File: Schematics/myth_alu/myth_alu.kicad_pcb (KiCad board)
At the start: 2 copper layers, 29 parts, among them J1 Conn_01x08_Pin, J2 Conn_01x08_Pin, J3 Conn_01x08_Pin, J4 Conn_01x08_Pin, J5 Conn_01x08_Pin, J6 Conn_01x08_Pin, J7 Conn_01x08_Pin, U1 74AHC273, U10 74AHC244, U11 74HC283, U12 74HC283, U13 74HC157, U14 74HC157, U15 74LS32, U16 74AHC273, U17 74AHC244, U18 4075, U19 74HC157, U2 74AHC273, U20 74HC283, U21 74HC283, U22 74AHC574, U3 SST39SF040, U4 74HC04, U5 SST39SF040, U6 74LS21, U7 74LS08, U8 74AHC273, U9 4078

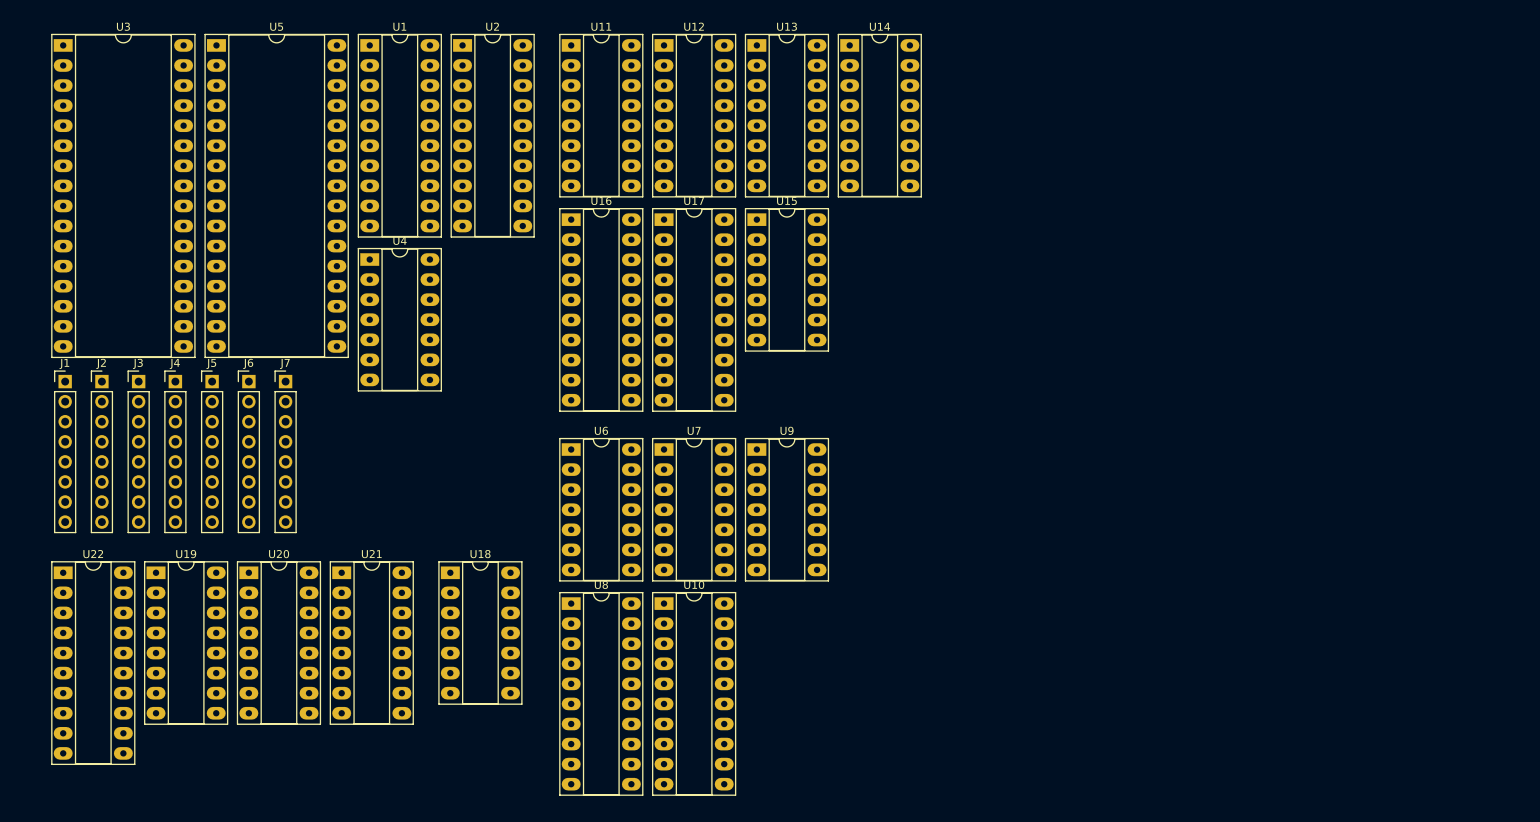
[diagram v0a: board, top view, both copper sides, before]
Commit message: Change d to g
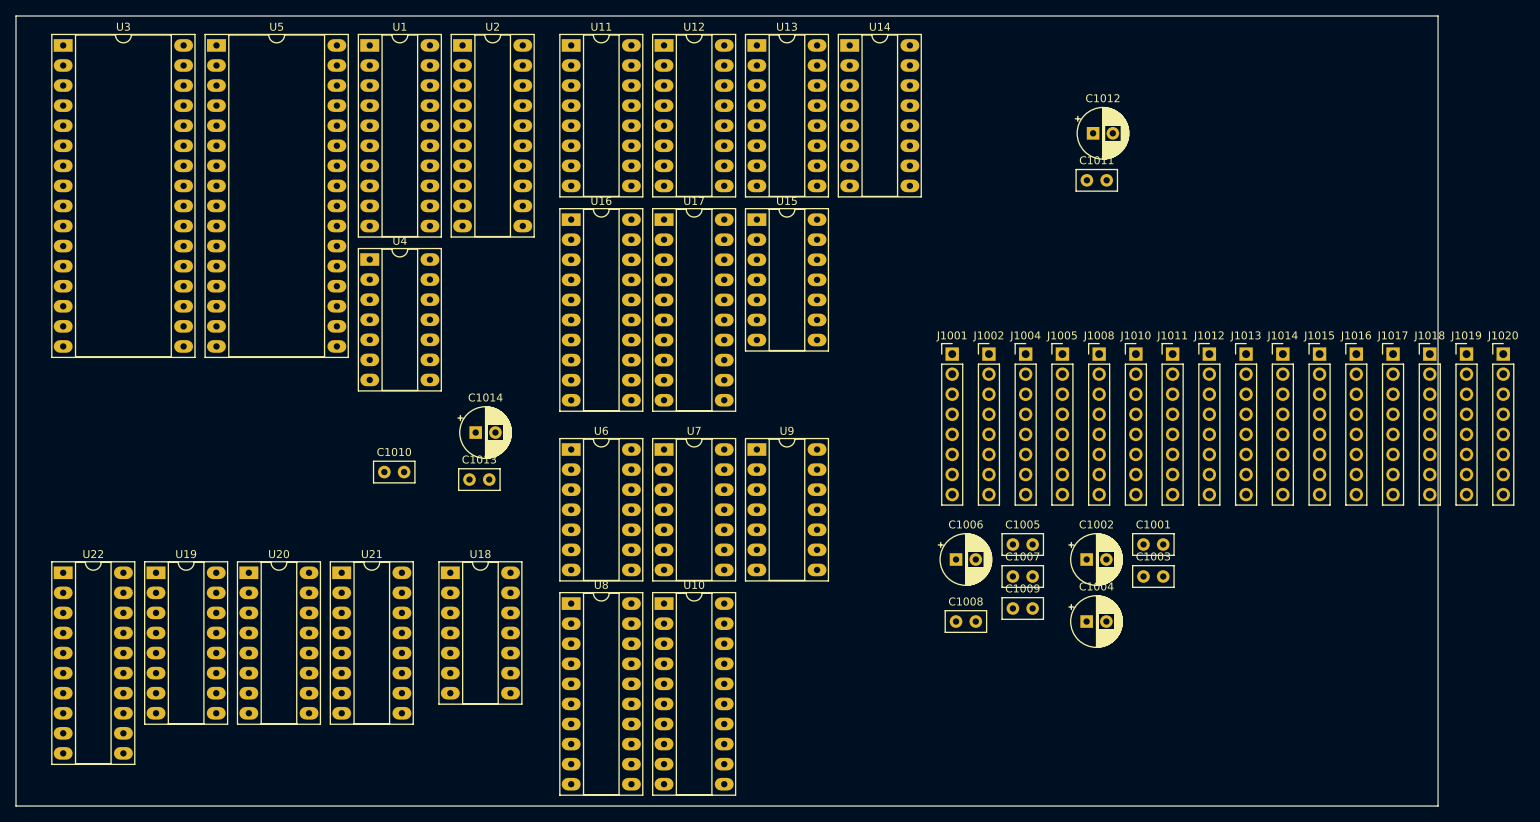
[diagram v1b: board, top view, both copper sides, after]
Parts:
- removed J1, J2, J3, J4, J5, J6, J7: Conn_01x08_Pin, Connector_PinHeader_2.54mm:PinHeader_1x08_P2.54mm_Vertical
- added C1001: C 100nF, Capacitor_THT:C_Disc_D5.0mm_W2.5mm_P2.50mm, F.Cu at (158.3, 84.2)
- added C1002: CP 10μF, Capacitor_THT:CP_Radial_D6.3mm_P2.50mm, F.Cu at (151.1, 86.1)
- added C1003: C 100nF, Capacitor_THT:C_Disc_D5.0mm_W2.5mm_P2.50mm, F.Cu at (158.3, 88.2)
- added C1004: CP 10μF, Capacitor_THT:CP_Radial_D6.3mm_P2.50mm, F.Cu at (151.1, 93.9)
- added C1005: C 100nF, Capacitor_THT:C_Disc_D5.0mm_W2.5mm_P2.50mm, F.Cu at (141.7, 84.2)
- added C1006: CP 10μF, Capacitor_THT:CP_Radial_D6.3mm_P2.50mm, F.Cu at (134.5, 86.1)
- added C1007: C 100nF, Capacitor_THT:C_Disc_D5.0mm_W2.5mm_P2.50mm, F.Cu at (141.7, 88.2)
- added C1008: C 100nF, Capacitor_THT:C_Disc_D5.0mm_W2.5mm_P2.50mm, F.Cu at (134.5, 93.9)
- added C1009: C 100nF, Capacitor_THT:C_Disc_D5.0mm_W2.5mm_P2.50mm, F.Cu at (141.7, 92.3)
- added C1010: C 100nF, Capacitor_THT:C_Disc_D5.0mm_W2.5mm_P2.50mm, F.Cu at (62.2, 75.0)
- added C1011: C 100nF, Capacitor_THT:C_Disc_D5.0mm_W2.5mm_P2.50mm, F.Cu at (151.1, 38.1)
- added C1012: CP 10μF, Capacitor_THT:CP_Radial_D6.3mm_P2.50mm, F.Cu at (151.9, 32.1)
- added C1013: C 100nF, Capacitor_THT:C_Disc_D5.0mm_W2.5mm_P2.50mm, F.Cu at (73.0, 76.0)
- added C1014: CP 10μF, Capacitor_THT:CP_Radial_D6.3mm_P2.50mm, F.Cu at (73.7, 70.0)
- added J1001: Conn_01x08_Pin, Connector_PinHeader_2.54mm:PinHeader_1x08_P2.54mm_Vertical, F.Cu at (134.1, 60.1)
- added J1002: Conn_01x08_Pin, Connector_PinHeader_2.54mm:PinHeader_1x08_P2.54mm_Vertical, F.Cu at (138.7, 60.1)
- added J1004: Conn_01x08_Pin, Connector_PinHeader_2.54mm:PinHeader_1x08_P2.54mm_Vertical, F.Cu at (143.3, 60.1)
- added J1005: Conn_01x08_Pin, Connector_PinHeader_2.54mm:PinHeader_1x08_P2.54mm_Vertical, F.Cu at (148.0, 60.1)
- added J1008: Conn_01x08_Pin, Connector_PinHeader_2.54mm:PinHeader_1x08_P2.54mm_Vertical, F.Cu at (152.7, 60.1)
- added J1010: Conn_01x08_Pin, Connector_PinHeader_2.54mm:PinHeader_1x08_P2.54mm_Vertical, F.Cu at (157.3, 60.1)
- added J1011: Conn_01x08_Pin, Connector_PinHeader_2.54mm:PinHeader_1x08_P2.54mm_Vertical, F.Cu at (161.9, 60.1)
- added J1012: Conn_01x08_Pin, Connector_PinHeader_2.54mm:PinHeader_1x08_P2.54mm_Vertical, F.Cu at (166.6, 60.1)
- added J1013: Conn_01x08_Pin, Connector_PinHeader_2.54mm:PinHeader_1x08_P2.54mm_Vertical, F.Cu at (171.2, 60.1)
- added J1014: Conn_01x08_Pin, Connector_PinHeader_2.54mm:PinHeader_1x08_P2.54mm_Vertical, F.Cu at (175.9, 60.1)
- added J1015: Conn_01x08_Pin, Connector_PinHeader_2.54mm:PinHeader_1x08_P2.54mm_Vertical, F.Cu at (180.6, 60.1)
- added J1016: Conn_01x08_Pin, Connector_PinHeader_2.54mm:PinHeader_1x08_P2.54mm_Vertical, F.Cu at (185.2, 60.1)
- added J1017: Conn_01x08_Pin, Connector_PinHeader_2.54mm:PinHeader_1x08_P2.54mm_Vertical, F.Cu at (189.8, 60.1)
- added J1018: Conn_01x08_Pin, Connector_PinHeader_2.54mm:PinHeader_1x08_P2.54mm_Vertical, F.Cu at (194.5, 60.1)
- added J1019: Conn_01x08_Pin, Connector_PinHeader_2.54mm:PinHeader_1x08_P2.54mm_Vertical, F.Cu at (199.2, 60.1)
- added J1020: Conn_01x08_Pin, Connector_PinHeader_2.54mm:PinHeader_1x08_P2.54mm_Vertical, F.Cu at (203.8, 60.1)
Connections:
- net /CLOSE renamed CLOSE
- net /DB0 renamed DB0
- net /DB1 renamed DB1
- net /DB2 renamed DB2
- net /DB3 renamed DB3
- net /DB4 renamed DB4
- net /DB5 renamed DB5
- net /DB6 renamed DB6
- net /DB7 renamed DB7
- net /IB0 renamed IB0
- net /IB1 renamed IB1
- net /IB2 renamed IB2
- net /IB3 renamed IB3
- net /O0 renamed O0
- net /O1 renamed O1
- net /O2 renamed O2
- net /O3 renamed O3
- net /O4 renamed O4
- net /O5 renamed O5
- net /O6 renamed O6
- net /O7 renamed O7
- net /R0 renamed R0
- net /R1 renamed R1
- net /R2 renamed R2
- net /R3 renamed R3
- net /R4 renamed R4
- net /R5 renamed R5
- net /R6 renamed R6
- net /R7 renamed R7
- net /xA renamed xA
- net /~{IB3} renamed ~{IB3}
- net /~{PUTO} renamed ~{PUTO}
- net /~{RES} renamed ~{RES}
- net /~{opc_ALU} renamed ~{opc_ALU}
- net /~{opc_FIX} renamed ~{opc_FIX}
- U11 pad 12: /ODEFER3 -> ODEFER3
- U11 pad 14: /ODEFER2 -> ODEFER2
- U11 pad 3: /ODEFER1 -> ODEFER1
- U11 pad 5: /ODEFER0 -> ODEFER0
- U12 pad 12: /ODEFER7 -> ODEFER7
- U12 pad 14: /ODEFER6 -> ODEFER6
- U12 pad 3: /ODEFER5 -> ODEFER5
- U12 pad 5: /ODEFER4 -> ODEFER4
- U12 pad 9: /xA_CARRY_OUT -> xA_CARRY_OUT
- U15 pad 2: /GETO -> GETO
- U15 pad 4: /xO -> xO
- U22 pad 11: /opc_FIX -> opc_FIX
- U6 pad 2: /~{GETR} -> ~{GETR}
- U6 pad 5: /~{xR} -> ~{xR}
- U7 pad 1: /~{PUTR} -> ~{PUTR}
- U7 pad 2: /Rx -> ~{Rx}
- U7 pad 5: /PH3 -> PH3
- U9 pad 1: /NZFLAG_R -> NZFLAG_R
- U9 pad 13: /ZFLAG_R -> ZFLAG_R
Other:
- board outline added: 180 x 100 mm
